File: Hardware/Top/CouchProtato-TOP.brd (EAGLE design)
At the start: 38 x 38 mm, 65 parts, among them SW1 SWITCH.MOM, SW2 SWITCH.MOM, U2 NRF52832_MODULE_MDBT42, U4 PCF8523, U5 FT231XS

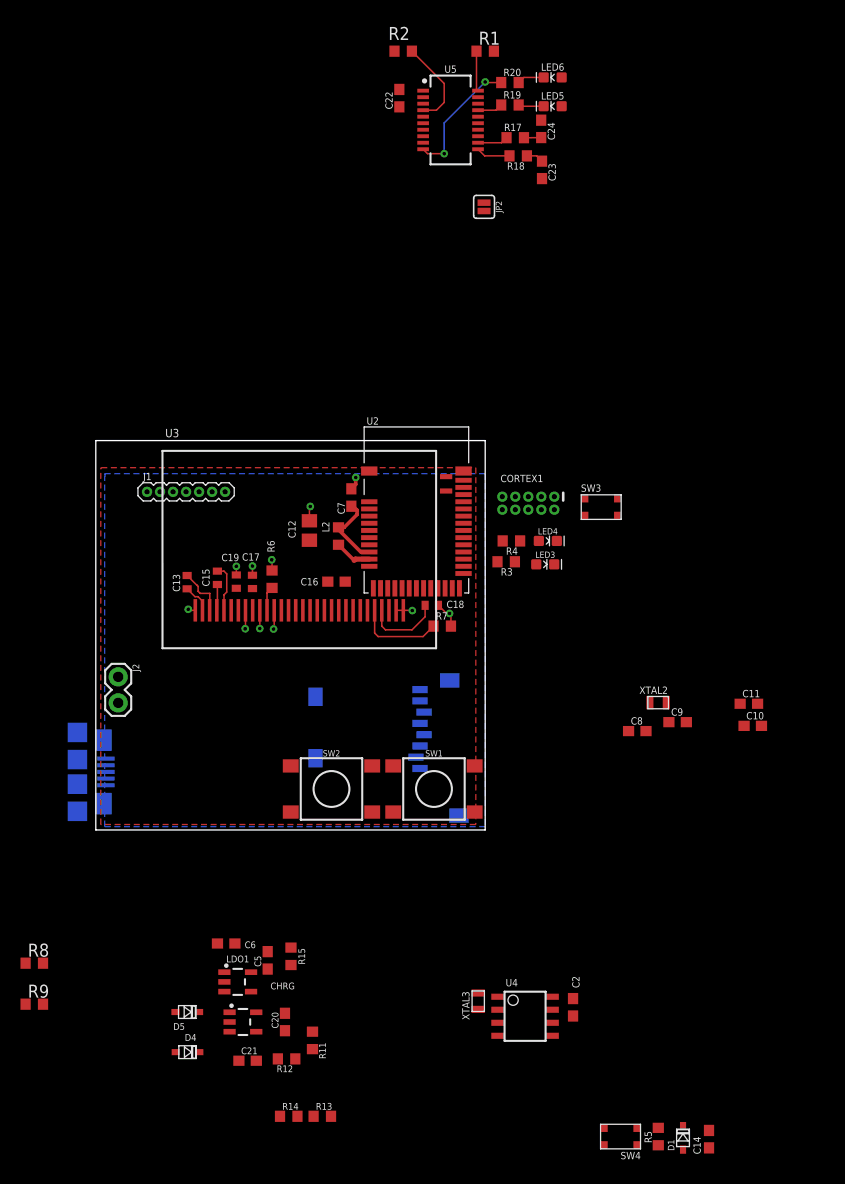
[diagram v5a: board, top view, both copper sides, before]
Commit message: Finished take 7, one more how to video to go, reorganizing and finalizing boards
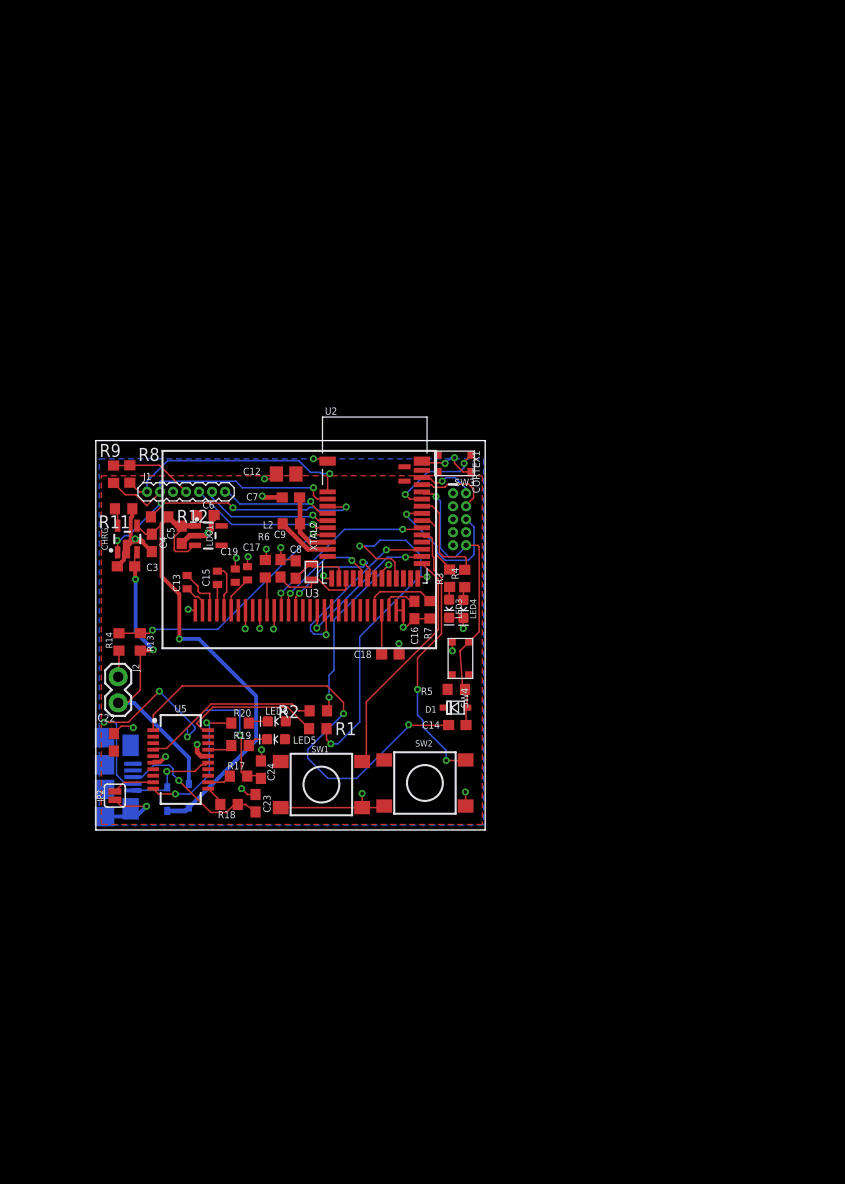
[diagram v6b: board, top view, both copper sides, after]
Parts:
- removed C10, C11: 300p, LinnesLab-Passives:C0603
- removed C2: 1u, LinnesLab-Passives:C0603
- removed C20, C21: 4.7u, LinnesLab-Passives:C0603
- removed R15: 100k, LinnesLab-Passives:R0603
- removed SD2: (no value), LinnesLab-Connectors:MICROSD
- removed U4: PCF8523, LinnesLab-Clocks:SO8
- removed XTAL3: 32.7680kHz, LinnesLab-Clocks:2-SMD.NOLEAD.2.0MMTO1.2MM
- added C3, C4: 4.7u, LinnesLab-Passives:C0603
- C18: device LinnesLab-Passives:C0402 -> LinnesLab-Passives:C0603
- moved R18 69.3 mm to (13.0, 2.49)
- moved C22 68.8 mm to (1.76, 8.55)
- moved LED6 68.4 mm to (17.7, 10.6)
- moved C24 68.3 mm to (16.1, 5.88)
- moved R1 68.1 mm to (21.7, 9.88)
- moved R17 67.9 mm to (13.9, 5.25)
- moved C23 67.8 mm to (15.6, 2.61), turned to 90 degrees
- moved R20 67.8 mm to (14.1, 10.4)
- moved R19 67.8 mm to (14.1, 8.24)
- moved JP2 67.8 mm to (1.86, 3.35), turned to 90 degrees
- moved U5 67.7 mm to (8.28, 6.88)
- moved LED5 67.4 mm to (17.6, 8.86)
- moved R2 64.9 mm to (21.7, 11.6), turned to 0 degrees
- moved R11 55.1 mm to (2.72, 31.3), turned to 180 degrees
- moved R12 54.3 mm to (6.22, 30.6), turned to 0 degrees
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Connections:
- removed net !DTR: U5.1
- removed net A4/BATT: R13.1, R14.2, U2.5
- removed net A6/TIA: J1.6, U2.7
- removed net A7/PPG: J1.7, U2.8
- removed net CD2: SD2.CD2
- removed net D29/LED.CTRL: J1.5, U2.6
- removed net N$19: U4.2, XTAL3.P$1
- removed net N$20: U4.1, XTAL3.P$2
- removed net VBAT: U4.3
- new net A4/PPG: J1.7, U2.5
- new net A5/TIA: J1.6, U2.6
- new net A7/BATT: R13.1, R14.2, U2.8
- new net D30/LED.CTRL: J1.5, U2.7
- net 3.3V: no longer C2.1, R15.2, SD2.4, U4.8
- net D5/CD1: no longer SD2.CD1
- net D7/SD.CS: no longer SD2.2
- net DTR: now also U5.1
- net GND: now also C3.2, C4.1; no longer C10.2, C11.2, C2.2, C20.2, C21.1, R15.1, SD2.6, SD2.MT1, SD2.MT2, U4.4
- net MISO: no longer SD2.7
- net MOSI: no longer SD2.3
- net P0.09/NFC1: no longer C11.1
- net P0.10/NFC2: no longer C10.1
- net SCK: no longer SD2.5
- net SCL: no longer U4.6
- net SDA: no longer U4.5
- net VIN: now also C4.2; no longer C21.2
- net VLIPO: now also C3.1; no longer C20.1
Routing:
- net GND: track 16.0 -> 85.7 mm, vias 11 -> 29
- net VIN: track 0.00 -> 50.6 mm, vias 0 -> 1
- net DTR: track 0.00 -> 45.7 mm, vias 0 -> 2
- net RXD.NRF: track 0.00 -> 36.6 mm, vias 0 -> 2
- net USB-: track 1.69 -> 36.0 mm, vias 0 -> 4
- net RESET: track 0.00 -> 29.9 mm, vias 0 -> 1
- net VLIPO: track 0.00 -> 29.9 mm, vias 0 -> 2
- net D27/CHRG.STATUS: track 0.00 -> 29.3 mm, vias 0 -> 4
- net D15/SW2: track 0.00 -> 27.2 mm, vias 0 -> 2
- net SCL: track 0.00 -> 24.6 mm, vias 0 -> 1
- net A7/BATT: track 0.00 -> 24.4 mm, vias 0 -> 2
- net SDA: track 0.00 -> 24.1 mm, vias 0 -> 1
- net D11/SW1: track 0.00 -> 23.1 mm
- net MOSI: track 0.00 -> 18.6 mm, vias 0 -> 2
- net TXD.NRF: track 0.00 -> 18.3 mm, vias 0 -> 2
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
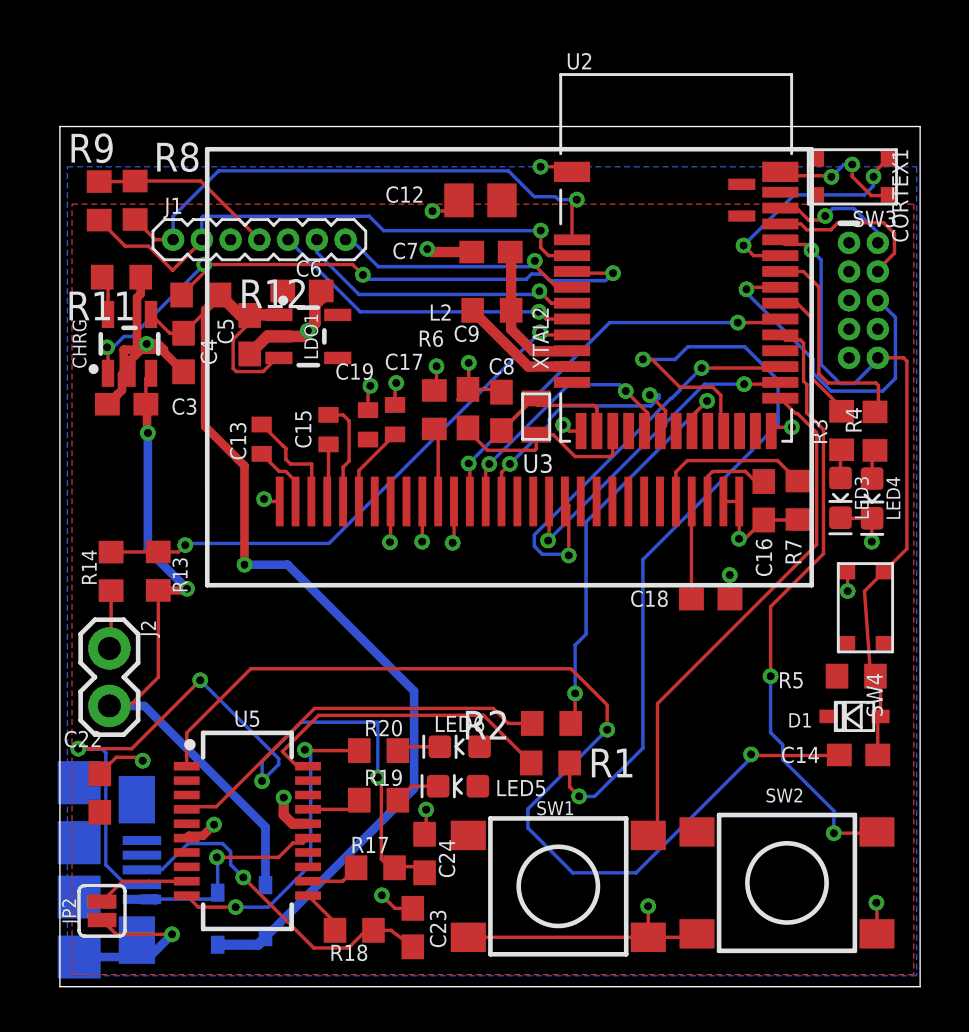
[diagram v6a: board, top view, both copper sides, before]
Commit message: Finished first revisions of EAGLE designs for smartwatch
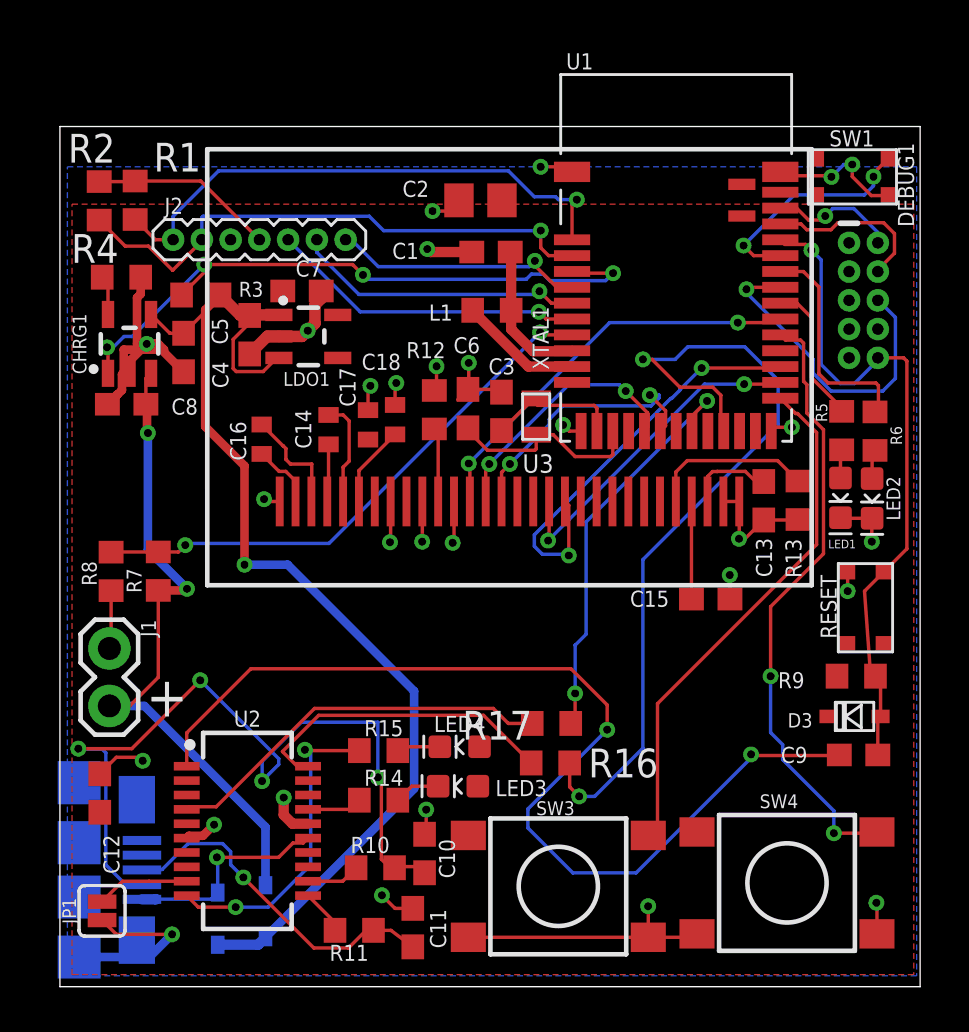
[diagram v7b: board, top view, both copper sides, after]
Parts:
- removed C19: 2.2uF, LinnesLab-Passives:C0402
- removed C22: 100n, LinnesLab-Passives:C0603
- removed D4: (no value), LinnesLab-DiscreteSemi:USC
- removed LED5: RED, LinnesLab-LED:LED-0603
- removed LED6: YELLOW, LinnesLab-LED:LED-0603
- removed R18: 27, LinnesLab-Passives:R0603
- removed R19: 1k, LinnesLab-Passives:R0603
- removed SW2: SWITCH.MOM, LinnesLab-Switches:TACTILE_SWITCH_SMD_6.2MM_TALL
- removed U5: FT231XS, LinnesLab-DigitalIC:SSOP20_L
- added C1: 1u, LinnesLab-Passives:C0603
- added C2: 10u, LinnesLab-Passives:C0805
- added D3: (no value), LinnesLab-DiscreteSemi:USC
- added LED1: RED, LinnesLab-LED:LED-0603
- added LED2: BLUE, LinnesLab-LED:LED-0603
- added R10: 27, LinnesLab-Passives:R0603
- added R16: 0, LinnesLab-Passives:R0603
- added RESET: (no value), LinnesLab-Switches:BUTTON-GULLWING
- added U1: NRF52832_MODULE_MDBT42, LinnesLab-Microcontrollers:BLE_MODULE_RAYTAC_MDBT42
- C12: value 10u -> 100n; device LinnesLab-Passives:C0805 -> LinnesLab-Passives:C0603
- C13: value 2.2uF -> 10uF; device LinnesLab-Passives:C0402 -> LinnesLab-Passives:C0603
- C14: value 100n -> 2.2uF; device LinnesLab-Passives:C0603 -> LinnesLab-Passives:C0402
- C15: device LinnesLab-Passives:C0402 -> LinnesLab-Passives:C0603
- C16: value 10uF -> 2.2uF; device LinnesLab-Passives:C0603 -> LinnesLab-Passives:C0402
- C18: device LinnesLab-Passives:C0603 -> LinnesLab-Passives:C0402
- C3: value 4.7u -> (none)
- C6: value 1u -> (none)
- C8: value (none) -> 4.7u
- C9: value (none) -> 100n
- J1: device LinnesLab-Connectors:1X07_1.27MM -> LinnesLab-Connectors:1X02
- J2: device LinnesLab-Connectors:1X02 -> LinnesLab-Connectors:1X07_1.27MM
- LED4: value BLUE -> YELLOW
- R1, R2: value 0 -> 10k
- R11: value (none) -> 27
- R12: value 100k -> 10k
- R13: value 100k -> 390k
- R14: value 100k -> 1k
- R17: value 27 -> 0
- R3: value 1k -> 100k
- R4: value 1k -> 5k
- R5, R6: value 10k -> 1k
- R7: value 390k -> 100k
- R8: value 10k -> 100k
- SW1: value SWITCH.MOM -> (none); device LinnesLab-Switches:TACTILE_SWITCH_SMD_6.2MM_TALL -> LinnesLab-Switches:BUTTON-GULLWING
- SW3, SW4: value (none) -> SWITCH.MOM; device LinnesLab-Switches:BUTTON-GULLWING -> LinnesLab-Switches:TACTILE_SWITCH_SMD_6.2MM_TALL
- U2: value NRF52832_MODULE_MDBT42 -> FT231XS; device LinnesLab-Microcontrollers:BLE_MODULE_RAYTAC_MDBT42 -> LinnesLab-DigitalIC:SSOP20_L
- moved R9 39.5 mm to (35.2, 13.7), turned to 180 degrees
- moved R4 34.0 mm to (2.72, 31.3), turned to 180 degrees
- moved SW1 33.9 mm to (35.0, 35.8)
- moved SW3 33.9 mm to (22.0, 4.43)
- moved U2 31.6 mm to (8.28, 6.88), turned to 270 degrees
- moved C12 31.1 mm to (1.76, 8.55), turned to 270 degrees
- moved R1 30.9 mm to (3.32, 34.7), turned to 90 degrees
- moved R11 30.6 mm to (13.0, 2.49)
- moved R2 30.5 mm to (1.73, 34.7), turned to 90 degrees
- moved R3 28.9 mm to (6.22, 30.6), turned to 0 degrees
- moved R13 28.4 mm to (32.6, 21.5)
- moved R7 28.4 mm to (4.34, 18.4)
- moved C14 27.5 mm to (11.9, 24.6), turned to 270 degrees
- moved D1 27.4 mm to (9.08, 3.34), flipped to the bottom, turned to 270 degrees
- moved C9 23.1 mm to (35.3, 10.2), turned to 0 degrees
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- renumbered C23 to C11, C24 to C10, CHRG to CHRG1, CORTEX1 to DEBUG1, D5 to D2, JP2 to JP1, L2 to L1, R20 to R15, USB2 to USB1, XTAL2 to XTAL1
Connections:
- net !CTS: now also U2.9; no longer U5.9
- net 3.3V: now also C18.2, C2.2, C7.1, D3.-, J2.4, LED3.A, LED4.A, R1.2, R2.2, U1.11, U2.14, U2.3; no longer C19.2, C22.2, C6.1, D1.-, J1.4, LED5.A, LED6.A, R5.2, R8.2, U2.11, U5.14, U5.3
- net A4/PPG: now also J2.7, U1.5; no longer J1.7, U2.5
- net A5/TIA: now also J2.6, U1.6; no longer J1.6, U2.6
- net A7/BATT: now also R7.1, R8.2, U1.8; no longer R13.1, R14.2, U2.8
- net D11/SW1: now also SW3.A1, U1.25; no longer SW1.A1, U2.25
- net D15/SW2: now also SW4.A1, U1.29; no longer SW2.A1, U2.29
- net D16/CS.OLED: now also U1.30; no longer U2.30
- net D27/CHRG.STATUS: now also R3.1, U1.4; no longer R12.1, U2.4
- net D3/RESET.OLED: now also U1.16; no longer U2.16
- net D30/LED.CTRL: now also J2.5, U1.7; no longer J1.5, U2.7
- net D4/DC.OLED: now also U1.17; no longer U2.17
- net D5/CD1: now also U1.18; no longer U2.18
- net D7/SD.CS: now also U1.20; no longer U2.20
- net DFU: now also SW1.3, U1.34; no longer SW3.3, U2.34
- net DTR: now also C9.1, U2.1; no longer C14.1, U5.1
- net FRST: now also U1.38; no longer U2.38
- net FT3V3: now also U2.13; no longer U5.13
- net GND: now also C1.2, C13.1, C15.1, C2.1, C3.1, C8.2, J1.1, J2.3, LED1.C, LED2.C, R12.1, R13.2, R4.1, R8.1, RESET.3, SW1.1, SW3.B1, SW3.B2, SW4.B1, SW4.B2, U1.1, U1.12, U1.24, U1.39, U2.16, U2.6; no longer C16.1, C19.1, C22.1, C3.2, C8.1, C9.2, J1.3, J2.1, LED3.C, LED4.C, R11.1, R14.1, R6.1, R7.2, SW1.B1, SW1.B2, SW2.B1, SW2.B2, SW3.1, SW4.3, U2.1, U2.12, U2.24, U2.39, U5.16, U5.6
- net LED1: now also R5.2, U1.31; no longer R3.2, U2.31
- net LED2: now also R6.2, U1.33; no longer R4.2, U2.33
- net MISO: now also U1.28; no longer U2.28
- net MOSI: now also U1.27; no longer U2.27
- net N$1: now also R12.2; no longer R6.2
- net N$10: now also LED2.A, R6.1; no longer LED4.A, R4.1
- net N$11: now also U1.10; no longer U2.10
- net N$12: now also C1.1, U1.9; no longer C7.1, U2.9
- net N$13: now also C13.2; no longer C16.2
- net N$15: now also C15.2; no longer C18.2
- net N$16: now also R4.2; no longer R11.2
- net N$2: now also R13.1; no longer R7.1
- net N$23: now also R10.2, U2.12; no longer R17.2, U5.12
- net N$24: now also R11.2, U2.11; no longer R18.2, U5.11
- net N$25: now also LED3.C, R14.2; no longer LED5.C, R19.2
- net N$26: now also LED4.C; no longer LED6.C
- net N$3: now also C16.2; no longer C13.2
- net N$4: now also C3.2, U1.13; no longer C8.2, U2.13
- net N$5: now also C16.1; no longer C13.1
- net N$6: now also C6.1, U1.14; no longer C9.1, U2.14
- net N$7: now also C14.2; no longer C15.2
- net N$8: now also C14.1; no longer C15.1
- net N$9: now also LED1.A, R5.1; no longer LED3.A, R3.1
- net P0.09/NFC1: now also U1.22; no longer U2.22
- net P0.10/NFC2: now also U1.23; no longer U2.23
- net RESET: now also C9.2, D3.+, R9.1, RESET.1, U1.35; no longer C14.2, D1.+, R5.1, SW4.1, U2.35
- net RXD.NRF: now also R16.2, U1.21; no longer R1.2, U2.21
- net RXDFT: now also R17.1, U2.4; no longer R2.1, U5.4
- net RXLED: now also R14.1, U2.17; no longer R19.1, U5.17
- net SCK: now also U1.26; no longer U2.26
- net SCL: now also J2.2, R2.1, U1.3; no longer J1.2, R9.1, U2.3
- net SDA: now also J2.1, R1.1, U1.2; no longer J1.1, R8.1, U2.2
- net SWCLK: now also U1.36; no longer U2.36
- net SWDIO: now also U1.37; no longer U2.37
- net SWO: now also U1.32; no longer U2.32
- net TXD.NRF: now also R17.2, U1.19; no longer R2.2, U2.19
- net TXDFT: now also R16.1, U2.20; no longer R1.1, U5.20
- net TXLED: now also U2.10; no longer U5.10
- net USB+: now also R11.1; no longer R18.1
- net USB-: now also R10.1; no longer R17.1
- net VIN: now also D1.-, R3.2; no longer D4.-, R12.2
- net VLIPO: now also C8.1, D1.+, J1.2, R7.2; no longer C3.1, D4.+, J2.2, R13.2
- net V_USB: now also U2.15; no longer U5.15
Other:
- board text added: "+"
